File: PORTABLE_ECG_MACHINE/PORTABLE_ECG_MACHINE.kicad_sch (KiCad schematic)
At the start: 55 parts, among them IC1 AD8232ACPZ, J1 USB_B_Micro, J2 Li-Ion 3.7 CONN, J3 UART, Q1 BSS138, Q2 BSS138, SW1 SW_SPDT, U1 CP2102-GM, U2 TP4056, U3 TC1262-33, U4 SSD1306

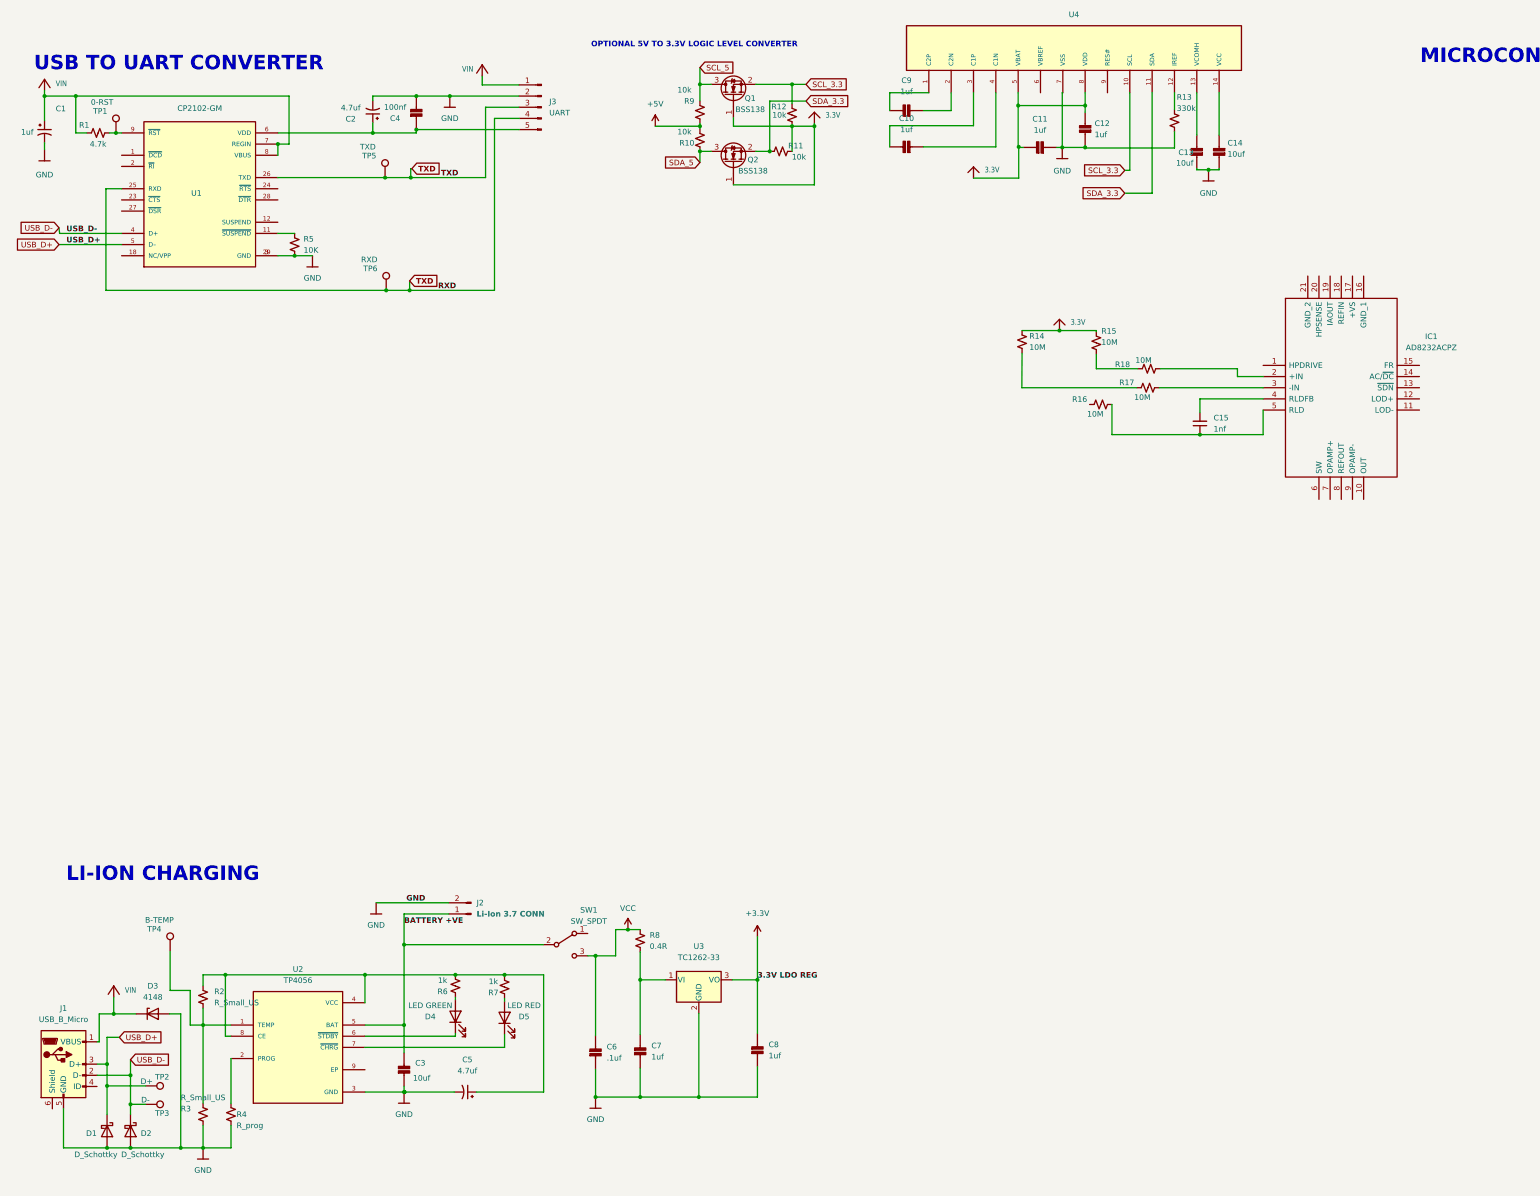
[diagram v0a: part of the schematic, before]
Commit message: OLED-INSTR_AMP-LION_CHAR-UART EESCHEMA UPDATE | PCBNEW ROUGH ARANGE
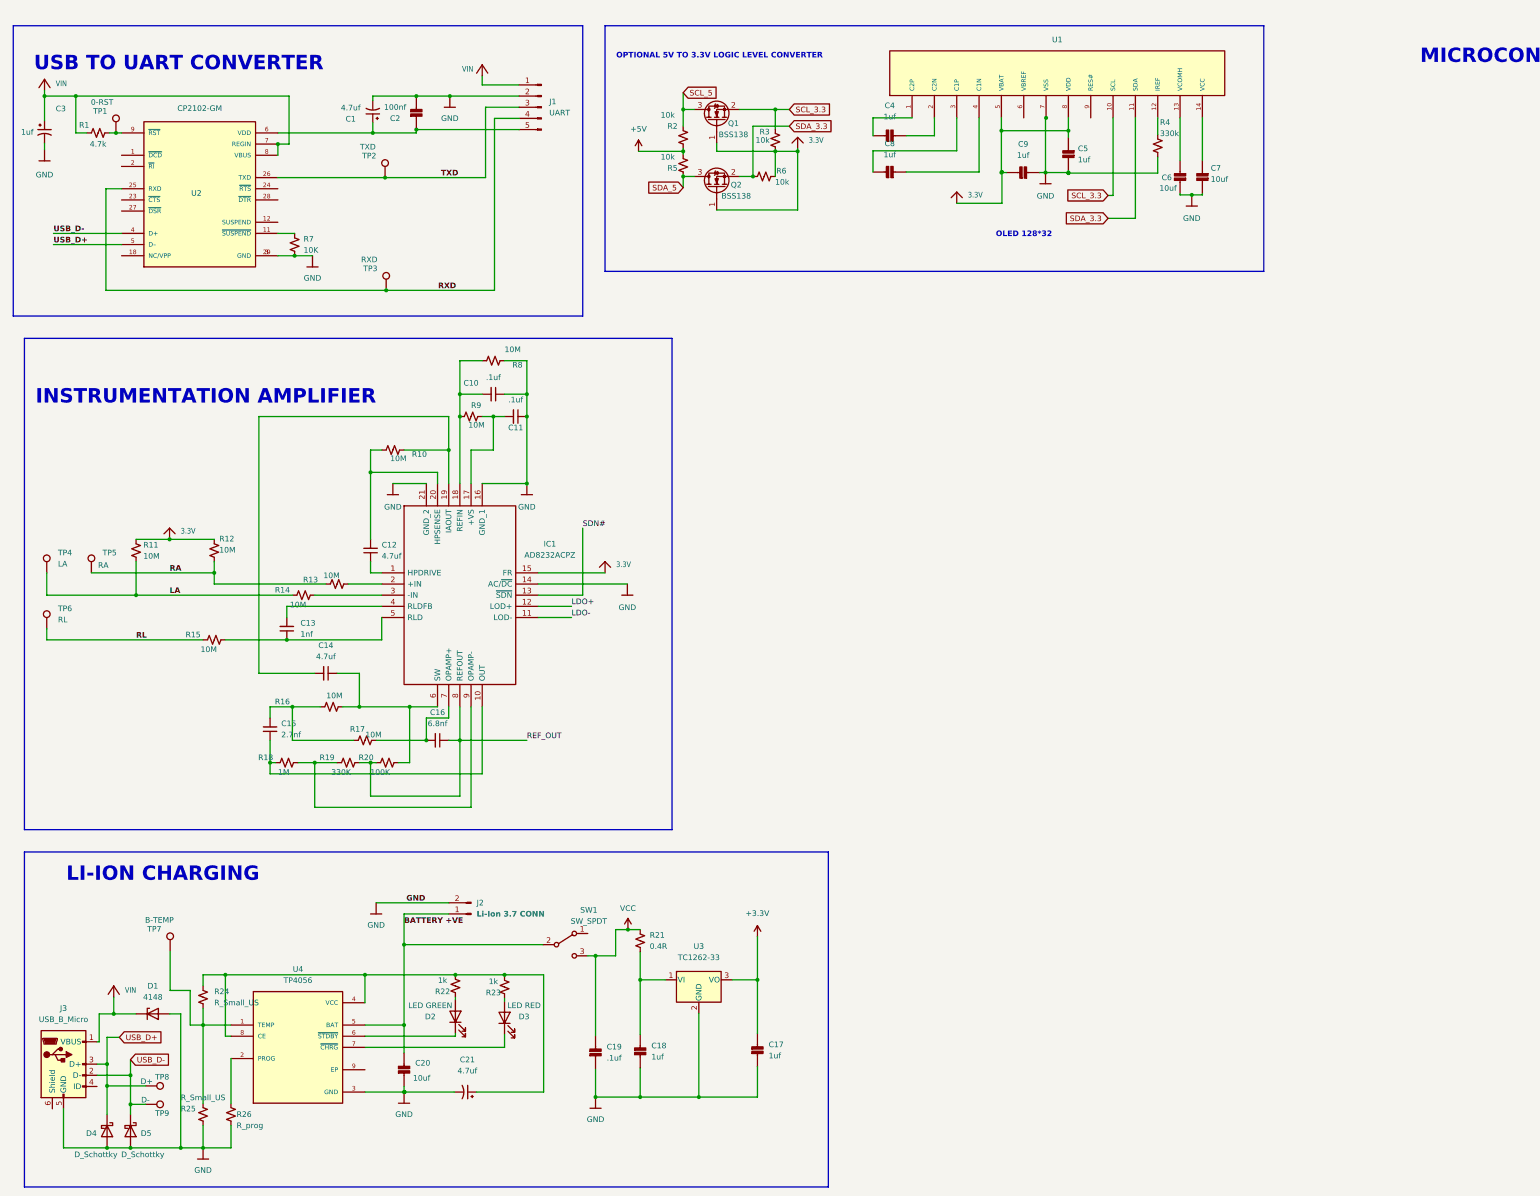
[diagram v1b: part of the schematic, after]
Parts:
- added C10, C11: .1uf, Capacitor_SMD:C_0603_1608Metric, symbol Device:C_Small
- added C12, C14: 4.7uf, Capacitor_SMD:C_0603_1608Metric, symbol Device:C_Small
- added C15: 2.7nf, Capacitor_SMD:C_0603_1608Metric, symbol Device:C_Small
- added C16: 6.8nf, Capacitor_SMD:C_0603_1608Metric, symbol Device:C_Small
- added R10, R16, R17, R8, R9: 10M, Resistor_SMD:R_0603_1608Metric, symbol Device:R_Small_US
- added R18: 1M, Resistor_SMD:R_0603_1608Metric, symbol Device:R_Small_US
- added R19: 330K, Resistor_SMD:R_0603_1608Metric, symbol Device:R_Small_US
- added R20: 100K, Resistor_SMD:R_0603_1608Metric, symbol Device:R_Small_US
- added TP4: LA, TestPoint:TestPoint_Pad_D1.0mm, symbol Connector:TestPoint
- added TP5: RA, TestPoint:TestPoint_Pad_D1.0mm, symbol Connector:TestPoint
- added TP6: RL, TestPoint:TestPoint_Pad_D1.0mm, symbol Connector:TestPoint
- U4: renamed from U2; footprint SOP127P600X175-9N -> Package_TO_SOT_SMD:TSOT-23-8
- renumbered C2 to C1, C15 to C13, C8 to C17, C7 to C18, C6 to C19, C4 to C2, C3 to C20, C5 to C21, C1 to C3, C9 to C4, C12 to C5, C13 to C6, C14 to C7, C10 to C8, C11 to C9, D3 to D1, D4 to D2, D5 to D3, D1 to D4, D2 to D5, J3 to J1, J1 to J3, R14 to R11, R15 to R12, R18 to R13, R17 to R14, R16 to R15, R9 to R2, R8 to R21, R6 to R22, R7 to R23, R2 to R24, R3 to R25, R4 to R26, R12 to R3, R13 to R4, R10 to R5, R11 to R6, R5 to R7, TP5 to TP2, TP6 to TP3, TP4 to TP7, TP2 to TP8, TP3 to TP9, U4 to U1, U1 to U2
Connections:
- net 3.3V: now also IC1.15 (FR)
- net GND: now also IC1.14 (AC/~{DC}), IC1.16 (GND_1), IC1.21 (GND_2), C10.1, C11.1, R8.1
- net TXD: no longer J1.4 (Pin_4), TP3.1, U2.25 (RXD)
- net LA: now reaches R11.2, R14.1
- net LA: now also TP4.1
- net at IC1.1 (HPDRIVE): now also C12.1
- net at IC1.10 (OUT): now also C15.1, R18.1
- net LDO-: now reaches IC1.11 (LOD-)
- net LDO+: now reaches IC1.12 (LOD+)
- net SDN#: now reaches IC1.13 (~{SDN})
- net at IC1.17 (+VS): now also C11.2, R9.1
- net at IC1.18 (REFIN): now also C10.2, R8.2, R9.2
- net at IC1.19 (IAOUT): now also C14.2, R10.1
- net at IC1.20 (HPSENSE): now also C12.2, R10.2
- net at IC1.6 (SW): now also C14.1, R16.2, R20.2
- net at IC1.7 (OPAMP+): now also C16.2, R17.2
- net REF_OUT: now reaches IC1.8 (REFOUT)
- net REF_OUT: now also C16.1, R19.2, R20.1
- net at IC1.9 (OPAMP-): now also R18.2, R19.1
- net RL: now reaches R15.1
- net RL: now also TP6.1
- net RA: now reaches R12.2, R13.1
- net RA: now also TP5.1
- new net: C15.2, R16.1, R17.1
- new net RXD: J1.4 (Pin_4), TP3.1, U2.25 (RXD)
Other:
- note added: "INSTRUMENTATION AMPLIFIER"
- note added: "OLED 128*32"
- moved on the sheet: C13, C4, C5, C6, C7, C8, C9, IC1, Q1, Q2, R11, R12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

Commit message: PCBNEW ROUGH STRUCTURE | EDGECUT PR
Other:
- moved on the sheet: R18
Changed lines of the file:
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@@
     (stroke (width 0) (type default) (color 0 0 0 0))
   )
-  (wire (pts (xy 80.01 182.88) (xy 83.82 182.88))
+  (wire (pts (xy 81.28 182.88) (xy 83.82 182.88))
     (stroke (width 0) (type default) (color 0 0 0 0))
   )
@@
     (stroke (width 0) (type default) (color 0 0 0 0))
   )
-  (wire (pts (xy 73.66 182.88) (xy 74.93 182.88))
+  (wire (pts (xy 73.66 182.88) (xy 76.2 182.88))
     (stroke (width 0) (type default) (color 0 0 0 0))
   )
@@
     (pin "2")
   )
-  (symbol (lib_id "Device:R_Small_US") (at 77.47 182.88 90) (unit 1)
-    (in_bom yes) (on_board yes)
-    (property "Reference" "R18" (id 0) (at 74.3712 181.7116 90)
-      (effects (font (size 1.27 1.27)) (justify left))
-    )
-    (property "Value" "1M" (id 1) (at 78.0796 185.0644 90)
-      (effects (font (size 1.27 1.27)) (justify left))
-    )
-    (property "Footprint" "Resistor_SMD:R_0603_1608Metric" (id 2) (at 77.47 182.88 0)
-      (effects (font (size 1.27 1.27)) hide)
-    )
-    (property "Datasheet" "~" (id 3) (at 77.47 182.88 0)
+  (symbol (lib_id "Device:R_Small_US") (at 78.74 182.88 90) (unit 1)
+    (in_bom yes) (on_board yes)
+    (property "Reference" "R18" (id 0) (at 75.6412 181.7116 90)
+      (effects (font (size 1.27 1.27)) (justify left))
+    )
+    (property "Value" "1M" (id 1) (at 79.3496 185.0644 90)
+      (effects (font (size 1.27 1.27)) (justify left))
+    )
+    (property "Footprint" "Resistor_SMD:R_0603_1608Metric" (id 2) (at 78.74 182.88 0)
+      (effects (font (size 1.27 1.27)) hide)
+    )
+    (property "Datasheet" "~" (id 3) (at 78.74 182.88 0)
       (effects (font (size 1.27 1.27)) hide)
     )
@@
   (symbol (lib_id "Device:R_Small_US") (at 87.63 170.18 90) (unit 1)
     (in_bom yes) (on_board yes)
-    (property "Reference" "R16" (id 0) (at 78.1812 169.0116 90)
-      (effects (font (size 1.27 1.27)) (justify left))
-    )
+    (property "Reference" "R16" (id 0) (at 88.9 172.72 90)
+      (effects (font (size 1.27 1.27)) (justify left))
+    )

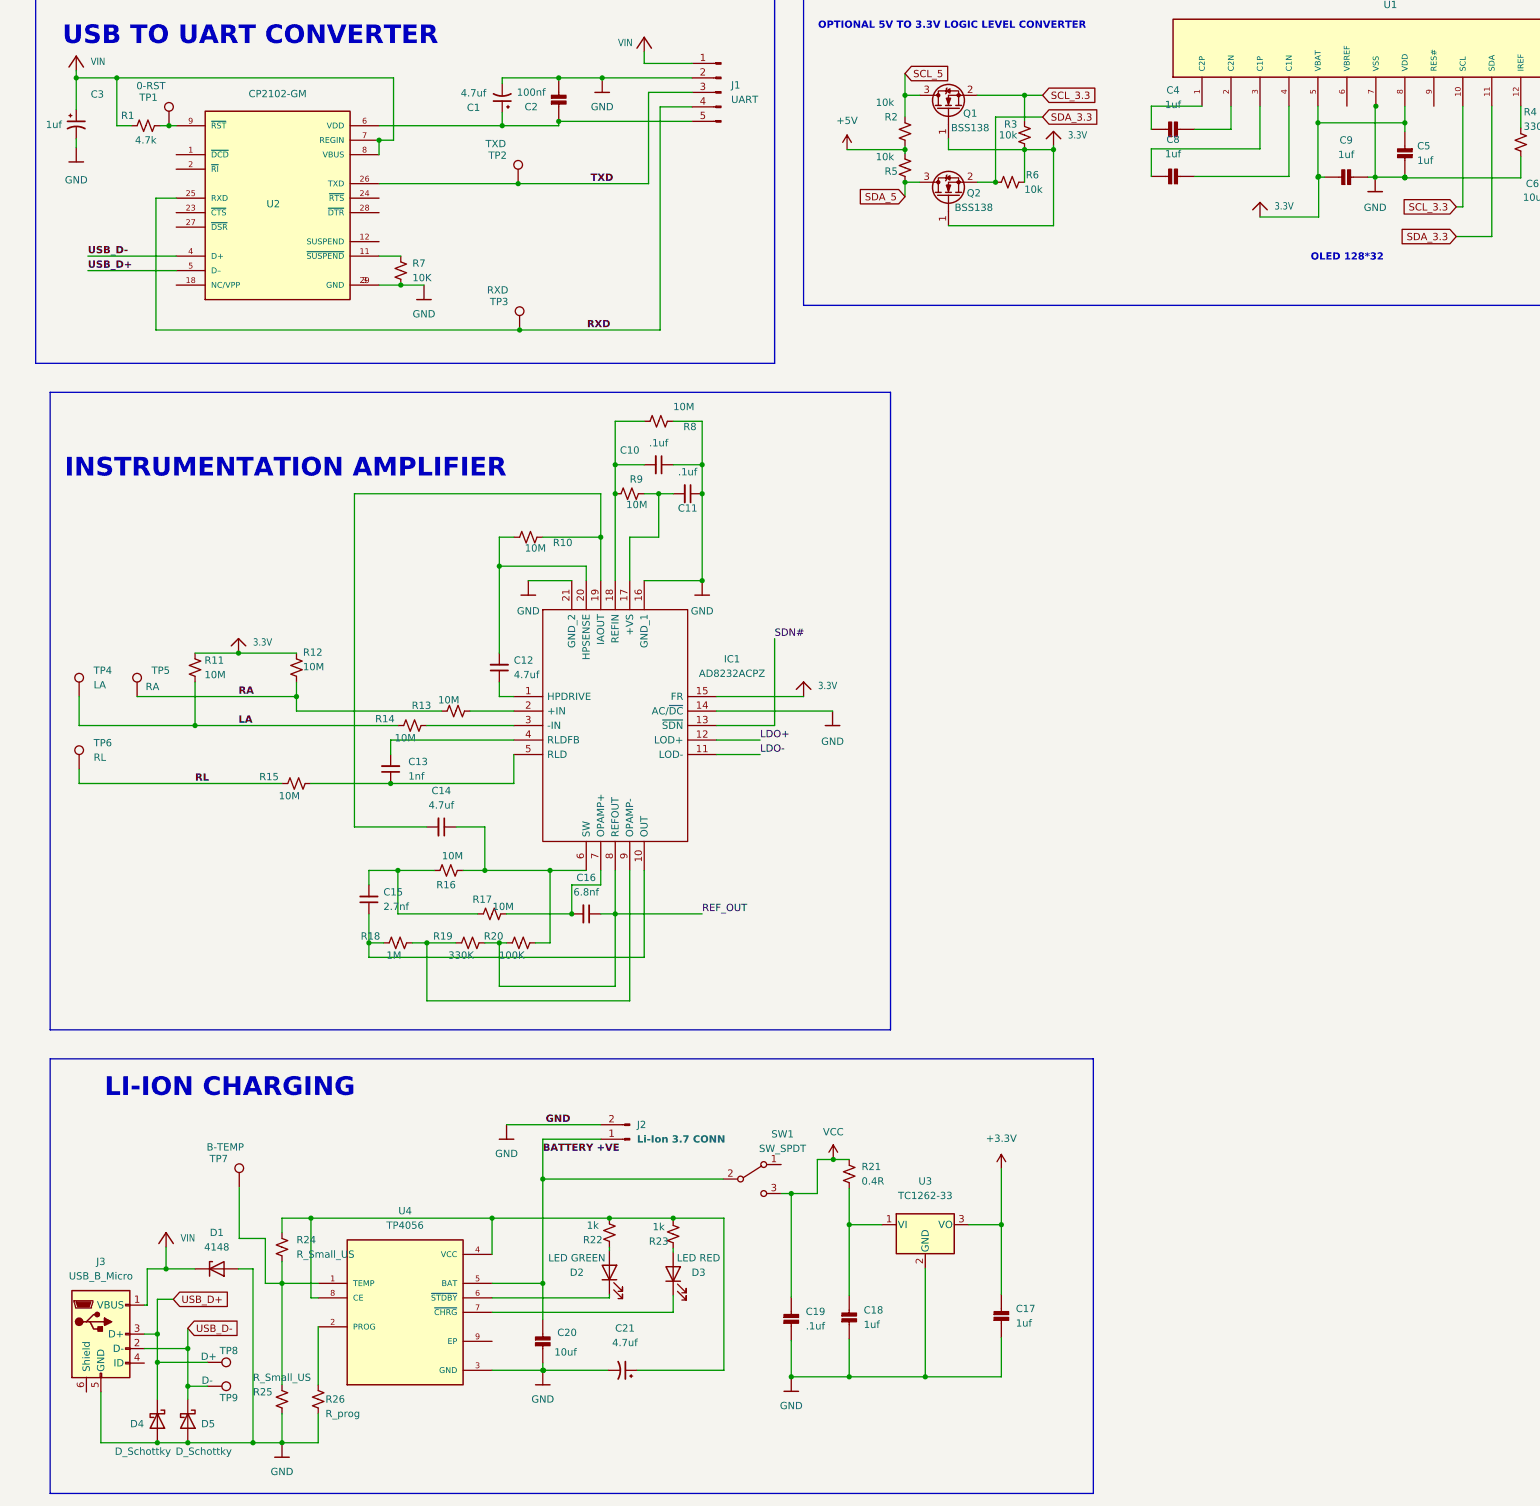
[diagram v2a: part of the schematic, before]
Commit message: PCBNEW LAYOUT FIX | ADD LIPO-USB_CONN-AUDIO_JACK-TACTILE SWITCH
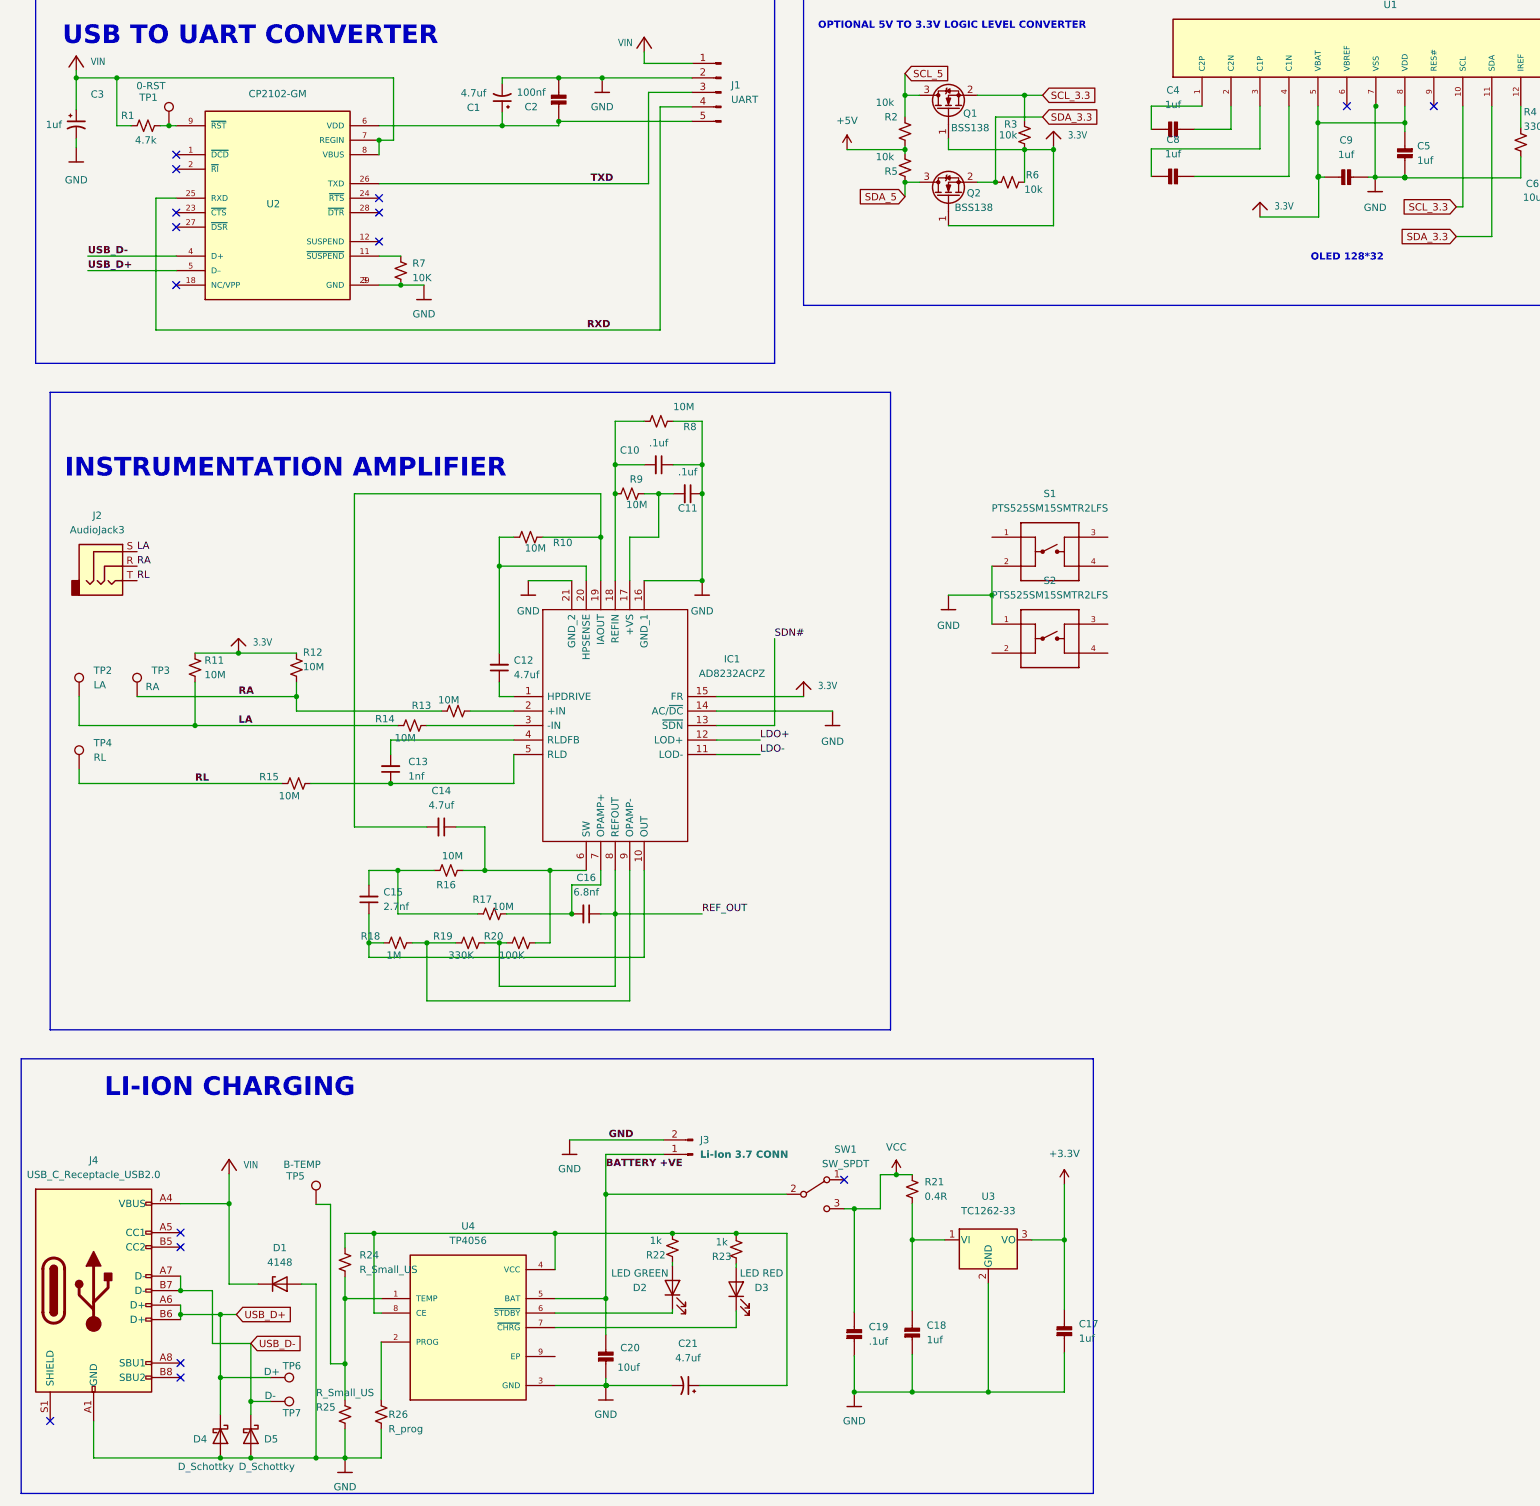
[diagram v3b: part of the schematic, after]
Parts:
- removed J3: USB_B_Micro, Connector_USB:USB_C_Receptacle_Amphenol_12401548E4-2A, symbol Connector:USB_B_Micro
- removed TP2: TXD, TestPoint:TestPoint_Pad_D1.0mm, symbol Connector:TestPoint
- removed TP3: RXD, TestPoint:TestPoint_Pad_D1.0mm, symbol Connector:TestPoint
- added J2: AudioJack3, Connector_Audio:Jack_3.5mm_CUI_SJ-3524-SMT_Horizontal, symbol Connector:AudioJack3
- added J4: USB_C_Receptacle_USB2.0, Connector_USB:USB_C_Receptacle_HRO_TYPE-C-31-M-12, symbol Connector:USB_C_Receptacle_USB2.0
- added S1, S2: PTS525SM15SMTR2LFS, SW_PTS525SM15SMTR2LFS, symbol tactile switch:PTS525SM15SMTR2LFS
- renumbered J2 to J3, TP4 to TP2, TP5 to TP3, TP6 to TP4, TP7 to TP5, TP8 to TP6, TP9 to TP7
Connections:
- net GND: now also J4.A1 (GND), J4.A12 (GND), J4.B1 (GND), J4.B12 (GND), S1.2, S2.1
- net LA: now also J2.S
- net RA: now also J2.R
- net RL: now also J2.T
- net USB_D+: now also J4.A6 (D+), J4.B6 (D+)
- net USB_D-: now also J4.A7 (D-), J4.B7 (D-)
- net VIN: now also J4.A4 (VBUS), J4.A9 (VBUS), J4.B4 (VBUS), J4.B9 (VBUS)
- net at R24.2, R25.2, U4.1 (TEMP): now also TP5.1
- no-connect marks 0 -> 16
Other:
- moved on the sheet: C17, C18, C19, C20, C21, D1, D2, D3, D4, D5, J3, R21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
